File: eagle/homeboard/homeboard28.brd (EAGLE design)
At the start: 94 x 71.8 mm, 126 parts, among them IC1 XCF02S, IC2 25LC080SN, IC3 ATMEGA32U2-TQFP, Q5 BC848SMD, Q6 BC848SMD, Q7 BC848SMD, Q8 BC848SMD, T1 BSS138, T2 BC848, T3 BSS138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

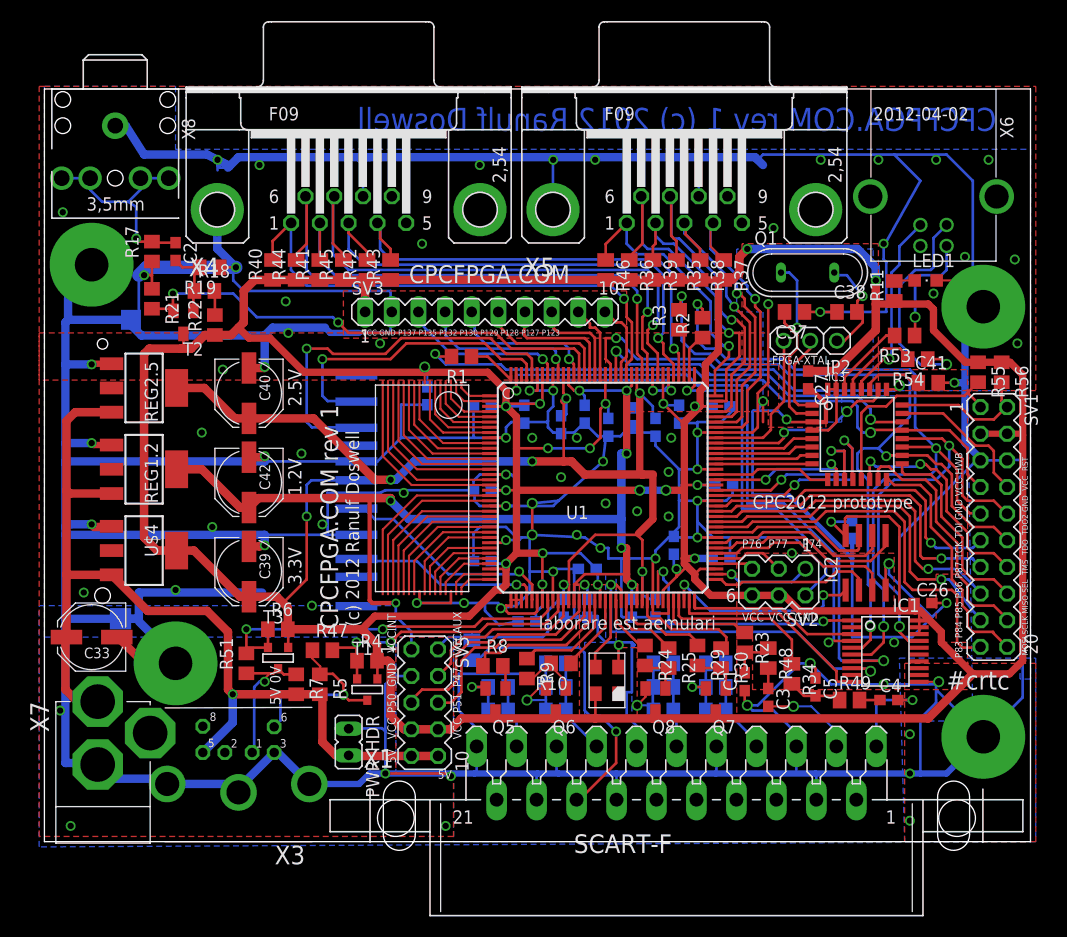
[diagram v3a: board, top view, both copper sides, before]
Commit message: move to 7mil
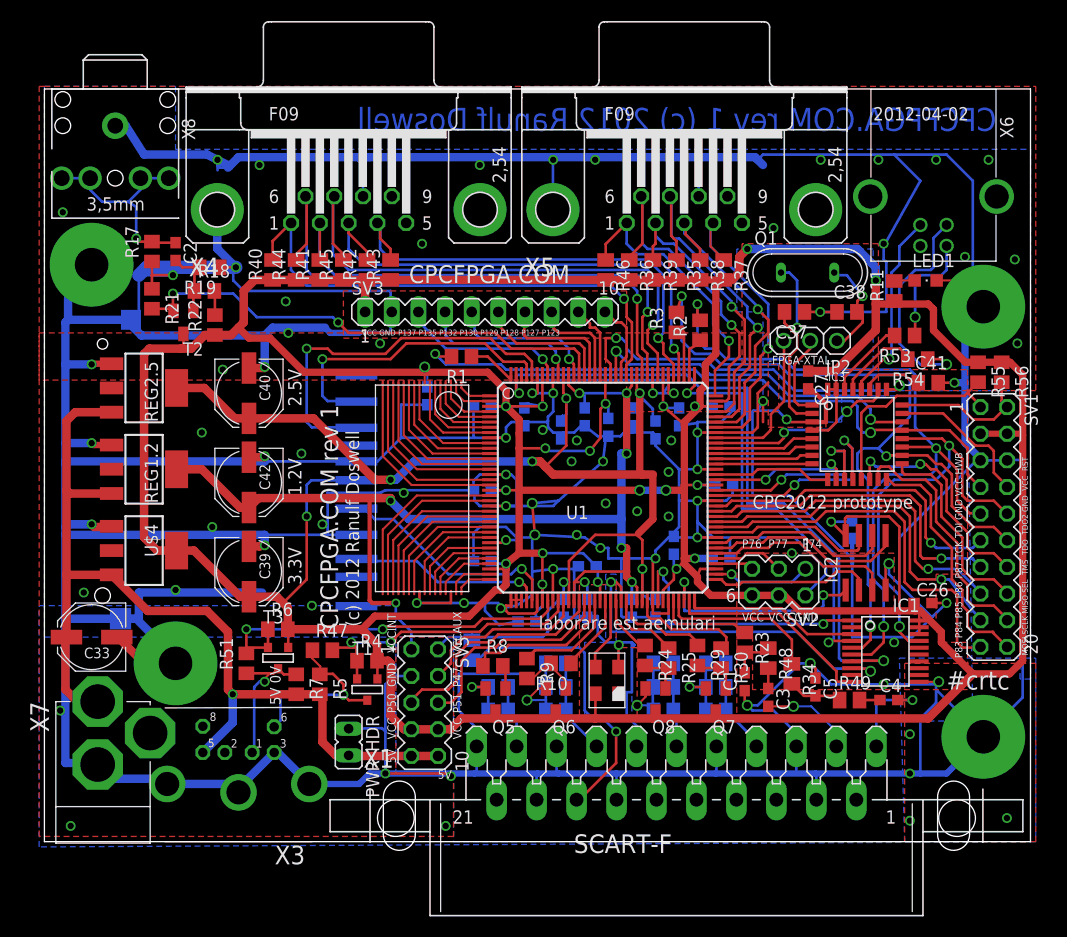
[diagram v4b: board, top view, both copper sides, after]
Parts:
- moved C19 0.50 mm to (49.2, 39.2)
- moved R2 0.35 mm to (62.5, 48.8)
- moved R3 0.35 mm to (60.2, 49.5)
- moved C12 0.25 mm to (45.8, 40.5)
- moved C15 0.25 mm to (51.8, 26.2)
- moved C20 0.25 mm to (58.2, 39.2)
- moved C22 0.25 mm to (51.5, 40.5)
- moved C7 0.25 mm to (60.5, 40.5)
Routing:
- net VCCAUX: track 122.7 -> 124.8 mm
- net FL_SEL: track 19.3 -> 21.2 mm
- net GND: track 1037.5 -> 1036.0 mm, vias 89 -> 88
- net N$39: track 4.88 -> 3.98 mm
- net JOY1_LEFT: track 28.9 -> 29.8 mm
- net N$40: track 64.7 -> 65.4 mm
- net PS2CLK: track 27.4 -> 28.1 mm
- net JOY1_FIRE1: track 33.0 -> 33.7 mm
- net JOY1_RIGHT: track 29.0 -> 29.6 mm
- net JOY1_FIRE2: track 33.4 -> 32.8 mm
- net VCC: track 545.9 -> 546.5 mm
- net SD_CLK: track 21.5 -> 22.0 mm
- net PROM_INITB: track 34.9 -> 35.4 mm
- net N$58: track 7.16 -> 7.66 mm

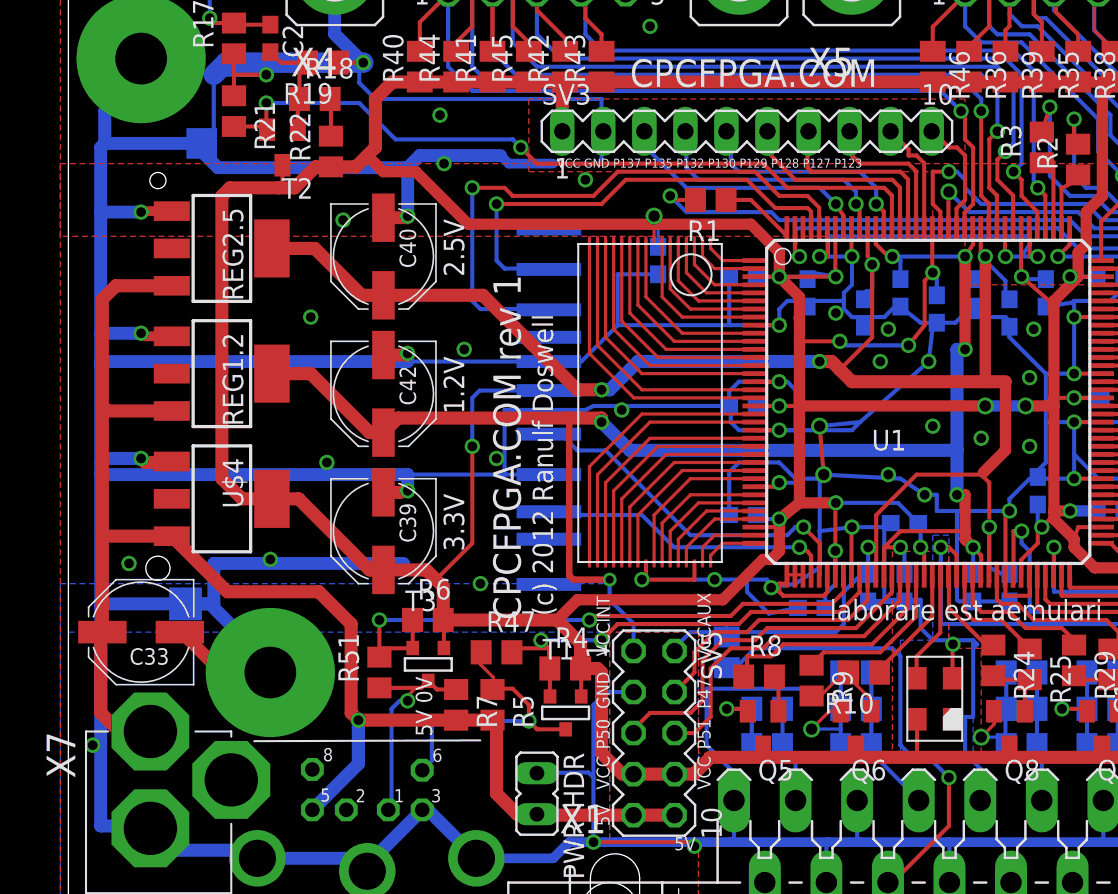
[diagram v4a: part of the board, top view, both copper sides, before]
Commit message: all at 7mil
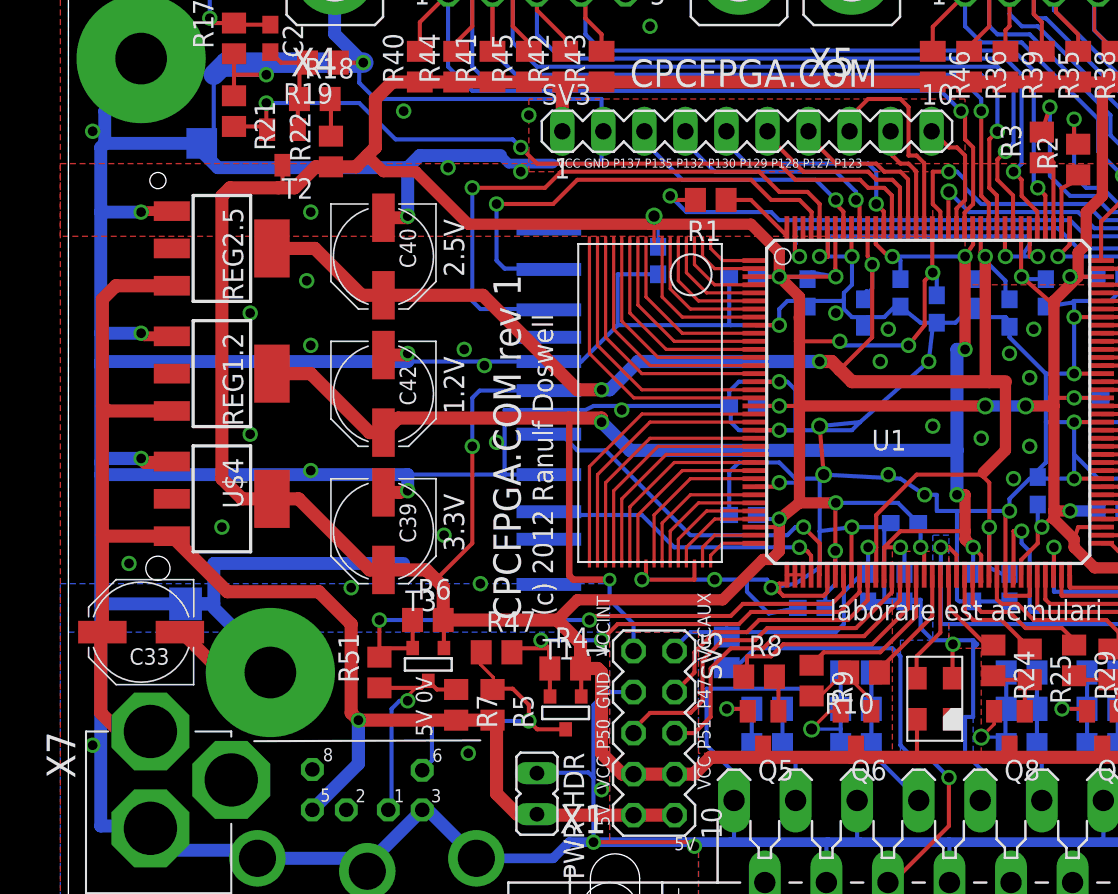
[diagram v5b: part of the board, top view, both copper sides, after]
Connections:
- net N$6: now also SV3.9; no longer SV3.8
- net N$7: now also SV3.8; no longer SV3.9
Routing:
- net N$7: track 7.20 -> 13.4 mm
- net N$6: track 9.51 -> 6.95 mm
- net N$5: track 11.9 -> 10.7 mm
- net N$1: track 15.8 -> 14.9 mm
- net N$4: track 13.0 -> 12.4 mm
- net GND: vias 88 -> 100
